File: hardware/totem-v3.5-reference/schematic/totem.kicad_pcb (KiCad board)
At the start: 4 copper layers, 45.8 x 46.4 mm, 136 parts, among them J1 USB4135-GF-A, J2 LiPo 1000mAh, J3 u.FL, Q1 AO3401A, Q2 2N7002, Q3 2N7002, Q4 AO3401A, Q5 2N7002, SW1 power, SW2 SOS, U1 ESP32-WROOM-32E, U2 MAX-M10S, U3 TP4056-42-ESOP8, U4 AP2112K-3.3, U5 ICM-20948

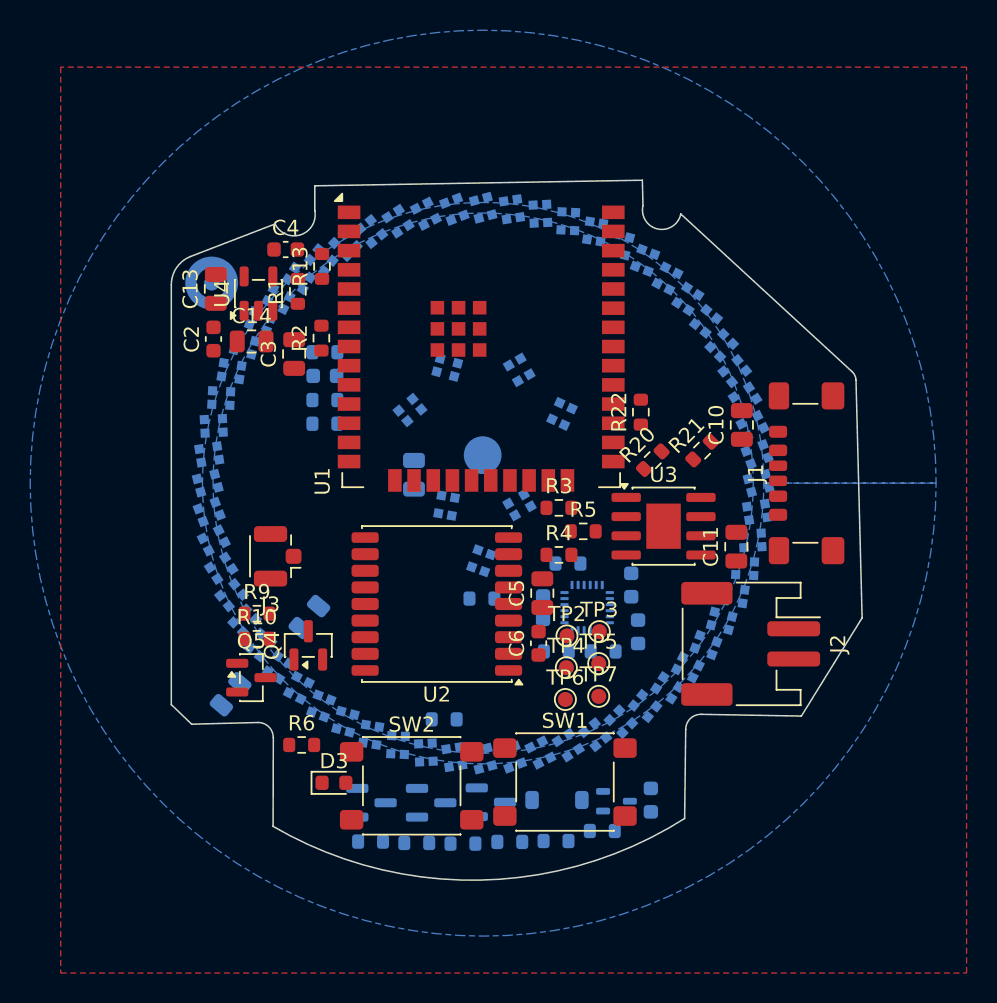
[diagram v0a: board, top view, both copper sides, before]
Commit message: feat: the board routed, DRC clean on every electrical check
route.py is a grid A* router over F.Cu and B.Cu with KiCad's own pad
polygons, per-class clearances from distance transforms, footprint rule
areas, and PathFinder-style history cost on rip-up; it converges to
every net routed, then checks connectivity itself. The LED side's VLED
pour is kept whole by a band no other net may cross; the one crossing
the ring's data needs (D100's DI faces out) is matched by feeding VLED
to D159 on the far side. The microphone uses a gapped GND ring
(mic_footprint.py) so its signal leaves on its own layer.

kicad-cli DRC: 0 unconnected, 0 clearance, 0 shorts, 0 narrow
connections, 0 keepout violations. Left: silkscreen warnings, the two
courtyard overlaps the photos show, and library-mismatch notes.

Docs: U5 and 'U6 I2948' were one chip seen from two angles; J1 carries
no data; the ring's LEDs are 1515s.

Claude-Session: https://claude.ai/code/session_0192KwQN6XkBBxwoQn8x3FMV
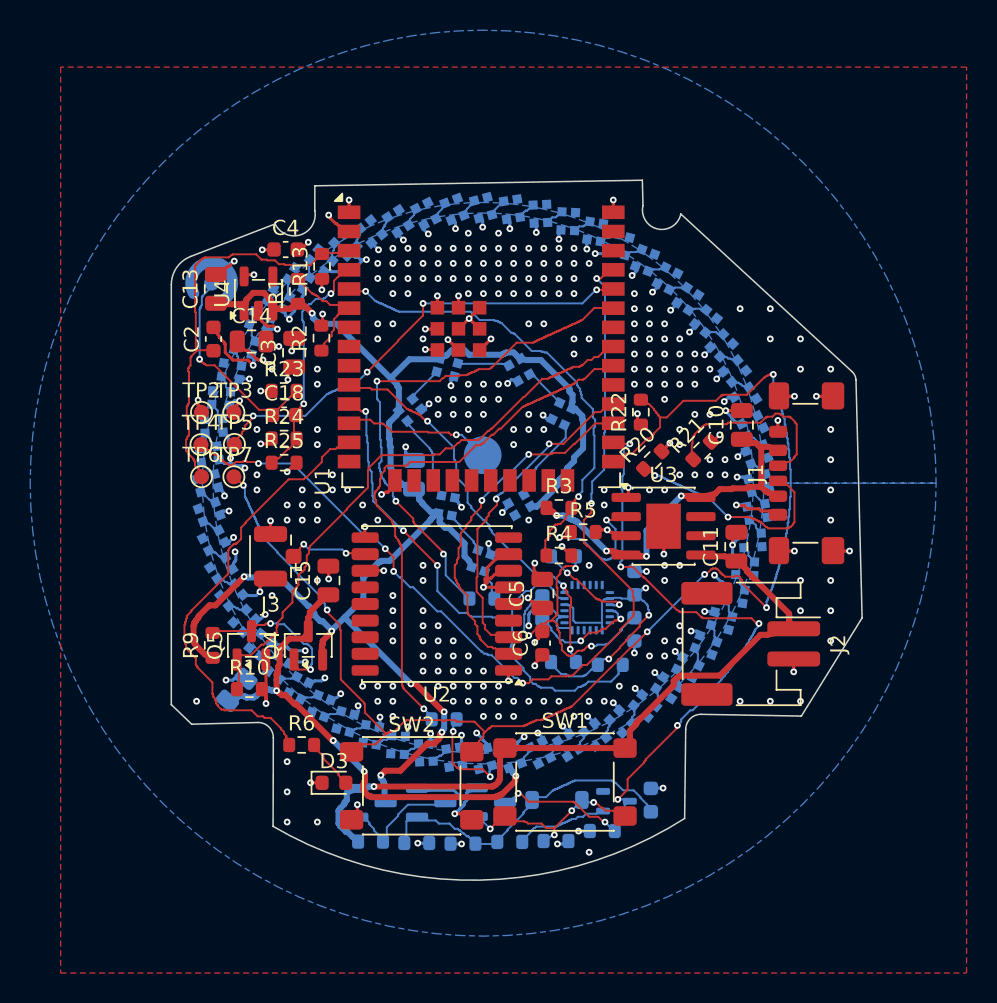
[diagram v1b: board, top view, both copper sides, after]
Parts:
- C15, C18, R23, R24, R25: moved to F.Cu
- MK1: footprint Sensor_Audio:CUI_CMC-4013-SMT -> totem:CUI_CMC-4013-SMT_RingGap
- moved TP2 28.4 mm to (79.3, 92.9)
- moved TP4 28.3 mm to (79.3, 95.0)
- moved TP6 28.3 mm to (79.3, 97.1)
- moved TP3 28.2 mm to (81.5, 92.9)
- moved TP7 28.2 mm to (81.5, 97.1)
- moved TP5 28.2 mm to (81.5, 95.0)
- moved C18 3.74 mm to (84.8, 93.0)
- moved R25 3.74 mm to (84.8, 96.2)
- moved R23 3.72 mm to (84.8, 91.4)
- moved R24 3.71 mm to (84.8, 94.6)
- moved R9 3.61 mm to (80.1, 108.3), turned to 90 degrees
- moved R10 3.37 mm to (82.5, 111.2)
- moved C15 2.73 mm to (87.7, 104.0), turned to 90 degrees
- moved Q5 2.14 mm to (82.6, 108.3), turned to 90 degrees
- moved R8 1.00 mm to (106.4, 109.6)
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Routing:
- net GND: track 0.00 -> 153.9 mm, vias 0 -> 338
- net VSYS: track 0.00 -> 101.4 mm, vias 0 -> 7
- net /BTN_SOS: track 0.00 -> 89.0 mm, vias 0 -> 6
- net /TXD0: track 0.00 -> 63.7 mm, vias 0 -> 6
- net VBAT: track 0.00 -> 48.1 mm, vias 0 -> 1
- net /GPIO4: track 0.00 -> 47.6 mm, vias 0 -> 7
- net +3V3: track 0.00 -> 40.4 mm, vias 0 -> 19
- net /LED_EN: track 0.00 -> 38.3 mm
- net /I2C0_SCL: track 0.00 -> 38.1 mm, vias 0 -> 3
- net /RING_DATA: track 0.00 -> 36.3 mm, vias 0 -> 1
- net /CRYSTAL_DATA: track 0.00 -> 34.7 mm, vias 0 -> 3
- net VLED: track 0.00 -> 33.1 mm, vias 0 -> 4
- net /VBUS_SENSE: track 0.00 -> 31.1 mm, vias 0 -> 2
- net /RXD0: track 0.00 -> 30.2 mm, vias 0 -> 4
- net /SOS_LED: track 0.00 -> 30.1 mm
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- removed copper zone on In2.Cu, net VLED

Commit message: fix: DRC clean with schematic parity, every check at every severity
- the LED footprint's pin mark moves to the ring's inner edge by DO, where
  the datasheet puts it and no neighbour's pad is
- references come off the silkscreen (0.3-0.4 mm between parts leaves no
  room); the fab layers and placement file keep them
- the gapped microphone footprint drops a silk circle that ran off the edge
- the three overlaps the reference board has (TP4056 by the module, SOS
  LED between the switch's legs) are narrow custom rules in
  totem.kicad_dru, each with its reason
- programming pads leave the BOM; the touch post's spring stays in it,
  and its comment now says what the photos show: an SMD spring, not a hole

kicad-cli pcb drc --schematic-parity --severity-all: 0 violations,
0 unconnected, 0 footprint errors. ERC 0/0.

Claude-Session: https://claude.ai/code/session_0192KwQN6XkBBxwoQn8x3FMV
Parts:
- TP1: value touch -> touch spring
